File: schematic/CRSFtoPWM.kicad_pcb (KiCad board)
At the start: 4 copper layers, 44.4 x 21.5 mm, 29 parts, among them J1 Bat+, J2 UART1/Rx, J3 ICSP, J4 TSW-104-08-G-T-RA, J5 TSW-104-08-G-T-RA, J6 TSW-104-08-G-T-RA, J7 TSW-102-08-L-T-RA, U1 AP7375-50W5-7, U2 AP2210N-3.3TRG1, U3 ATSAMD21E18A-MU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

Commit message: Pcb fully routed - needs optimization
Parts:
- moved R3 0.20 mm to (163.7, 111.3)
- moved R2 0.10 mm to (146.2, 112.3)
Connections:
- J4 pad 1: SCL -> +3V3
- J4 pad 2: +3V3 -> +5V
- J4 pad 4: SDA -> TX2
- J4 pad 5: GND -> RX2
- J4 pad 6: +5V -> GND
- J4 pad 7: RX2 -> SCL
- J4 pad 8: TX2 -> SDA
- U3 pad 16: unconnected-(U3-Pad16) -> Net-(R6-Pad1)
- U3 pad 19: Net-(R6-Pad1) -> unconnected-(U3-Pad19)
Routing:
- net Vservo: track 0.00 -> 70.5 mm
- net Vbat: track 0.00 -> 26.5 mm
- net SDA: track 0.00 -> 25.3 mm, vias 0 -> 1
- net SCL: track 0.00 -> 24.0 mm, vias 0 -> 3
- net GND: track 0.00 -> 21.6 mm, vias 0 -> 14
- net Net-(J2-Pad3): track 0.00 -> 20.8 mm, vias 0 -> 2
- net Net-(R1-Pad2): track 0.00 -> 20.7 mm, vias 0 -> 2
- net Net-(J3-Pad1): track 0.00 -> 20.3 mm, vias 0 -> 1
- net RX2: track 0.00 -> 20.0 mm, vias 0 -> 1
- net CH9: track 0.00 -> 19.5 mm
- net Net-(J2-Pad4): track 0.00 -> 19.4 mm, vias 0 -> 2
- net +5V: track 0.00 -> 18.6 mm
- net CH10: track 0.00 -> 17.6 mm
- net CH8: track 0.00 -> 17.0 mm
- net TX2: track 0.00 -> 16.5 mm, vias 0 -> 1
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- added copper zone on In2.Cu, net +3V3
- added copper zone on In1.Cu, net GND
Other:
- board size 44.4 x 21.5 mm -> 43.9 x 21.5 mm

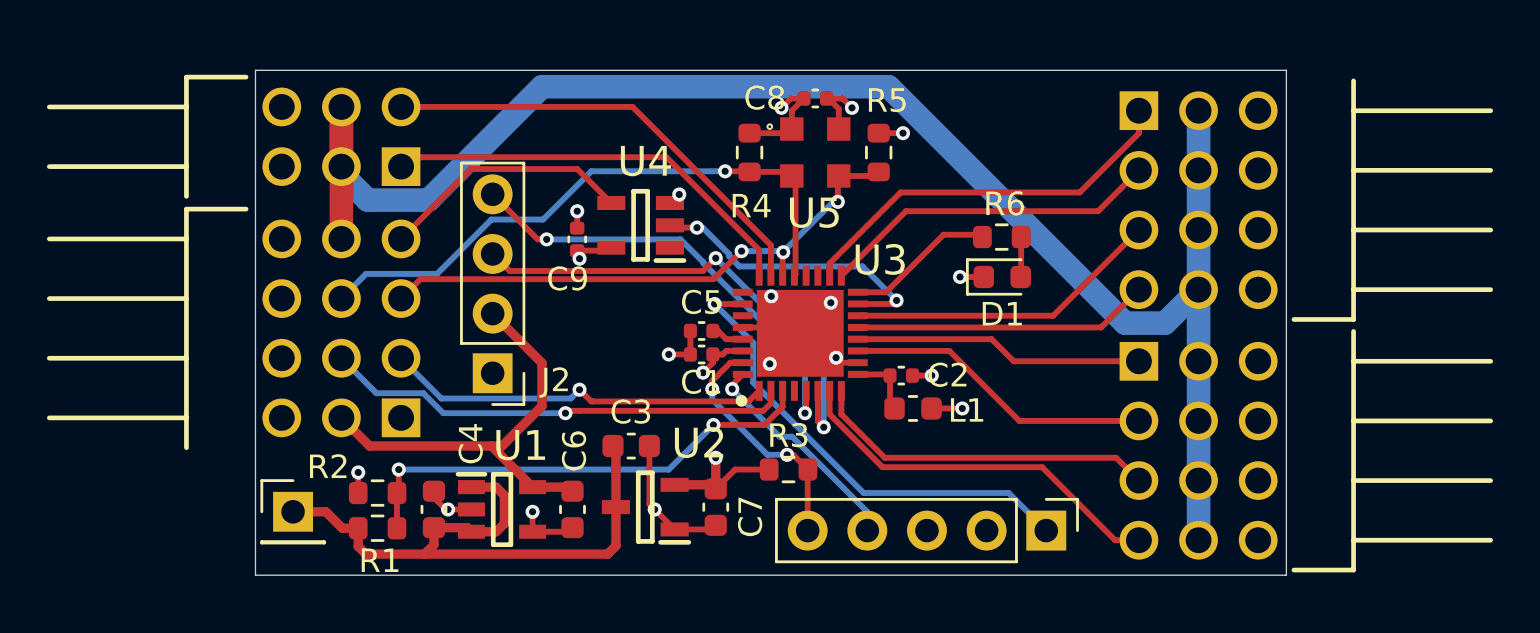
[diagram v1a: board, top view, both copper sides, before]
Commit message: Smaller pcb and tweaks
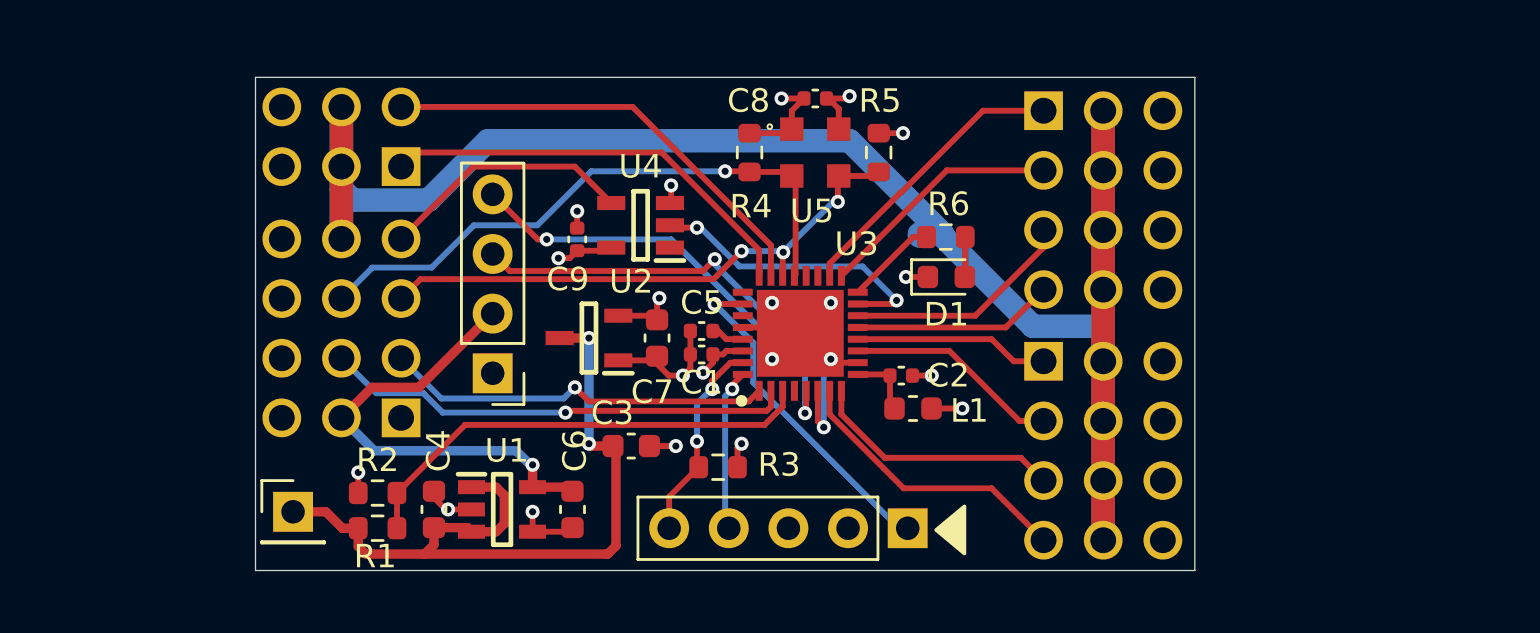
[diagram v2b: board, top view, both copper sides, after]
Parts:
- moved C7 7.62 mm to (158.1, 105.7)
- moved U2 7.59 mm to (155.2, 105.7)
- moved J3 5.90 mm to (168.8, 113.8)
- moved J5 4.06 mm to (174.6, 106.7)
- moved J6 4.06 mm to (174.6, 96.0)
- moved R3 3.00 mm to (160.7, 111.2), turned to 180 degrees
- moved D1 2.38 mm to (170.4, 103.1)
- moved R6 2.38 mm to (170.4, 101.4)
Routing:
- net Vservo: track 70.5 -> 84.8 mm
- net Vbat: track 26.5 -> 33.3 mm, vias 0 -> 2
- net Net-(U3-Pad26): track 20.3 -> 14.0 mm
- net CH8: track 17.0 -> 12.3 mm
- net CH5: track 16.4 -> 12.3 mm
- net CH7: track 14.5 -> 10.5 mm
- net CH6: track 14.8 -> 10.8 mm
- net CH3: track 12.6 -> 8.58 mm
- net CH2: track 12.4 -> 8.30 mm
- net CH1: track 13.2 -> 9.14 mm
- net CH4: track 13.5 -> 9.86 mm
- net Net-(J3-Pad4): track 9.53 -> 6.71 mm
- net Net-(R6-Pad1): track 6.22 -> 3.90 mm
- net Net-(J3-Pad5): track 10.3 -> 8.63 mm
- net +3V3: track 16.1 -> 14.5 mm, vias 6 -> 7
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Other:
- board size 43.9 x 21.5 mm -> 40 x 21 mm

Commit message: Added text, minor tweaks
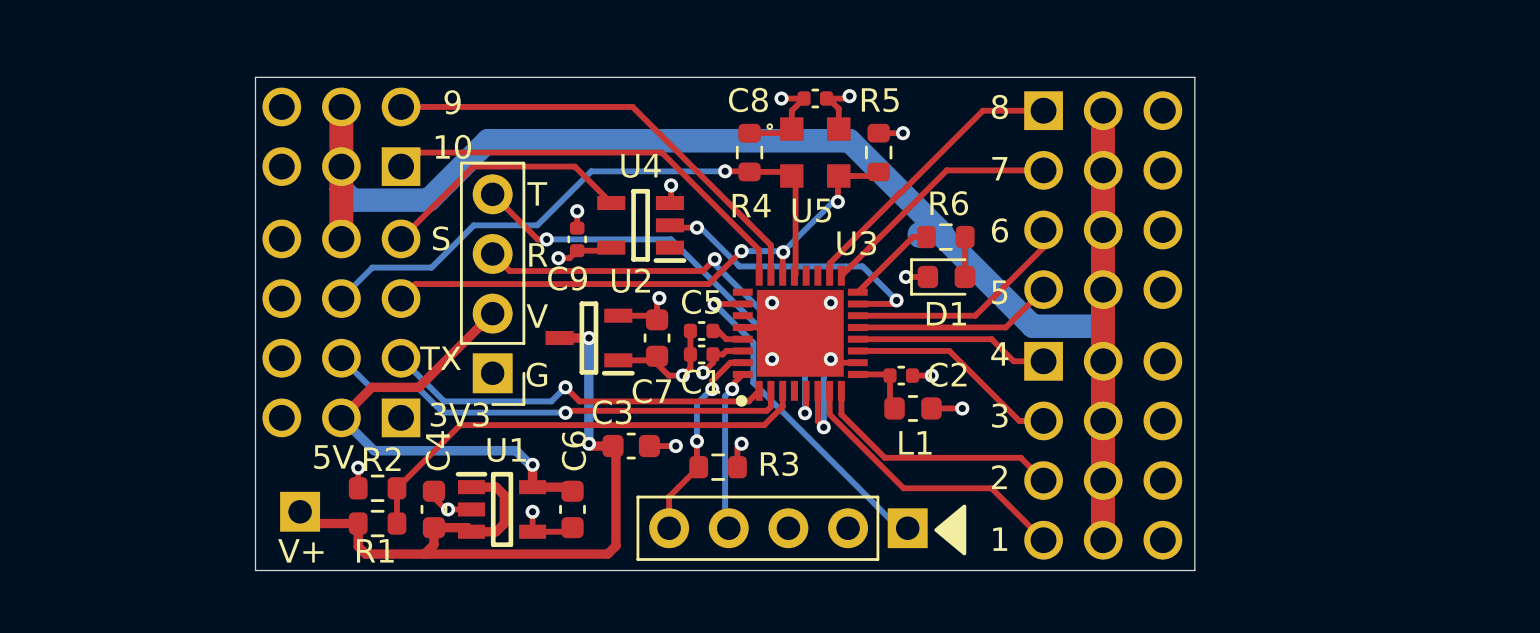
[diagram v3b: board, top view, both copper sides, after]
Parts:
- moved J1 0.30 mm to (142.9, 113.1)
- moved R1 0.20 mm to (146.2, 113.6)
- moved R2 0.20 mm to (146.2, 112.1)
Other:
- board text added: "+"
- board text added: "-"
- board text added: "1"
- board text added: "10"
- board text added: "2"
- board text added: "3"
- board text added: "3V3"
- board text added: "4"
- board text added: "5"
- board text added: "5V"
- board text added: "6"
- board text added: "7"
- board text added: "8"
- board text added: "9"
- board text added: "CRSFtoPWM"
- board text added: "G"
- board text added: "JLCJLCJLC"
- board text added: "R"
- board text added: "S"
- board text added: "T"
- board text added: "TX"
- board text added: "V"
- board text added: "V+"
- board text added: "V1.0 QES 2023"
- board text added: "s"

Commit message: Improved Vservo current capacity
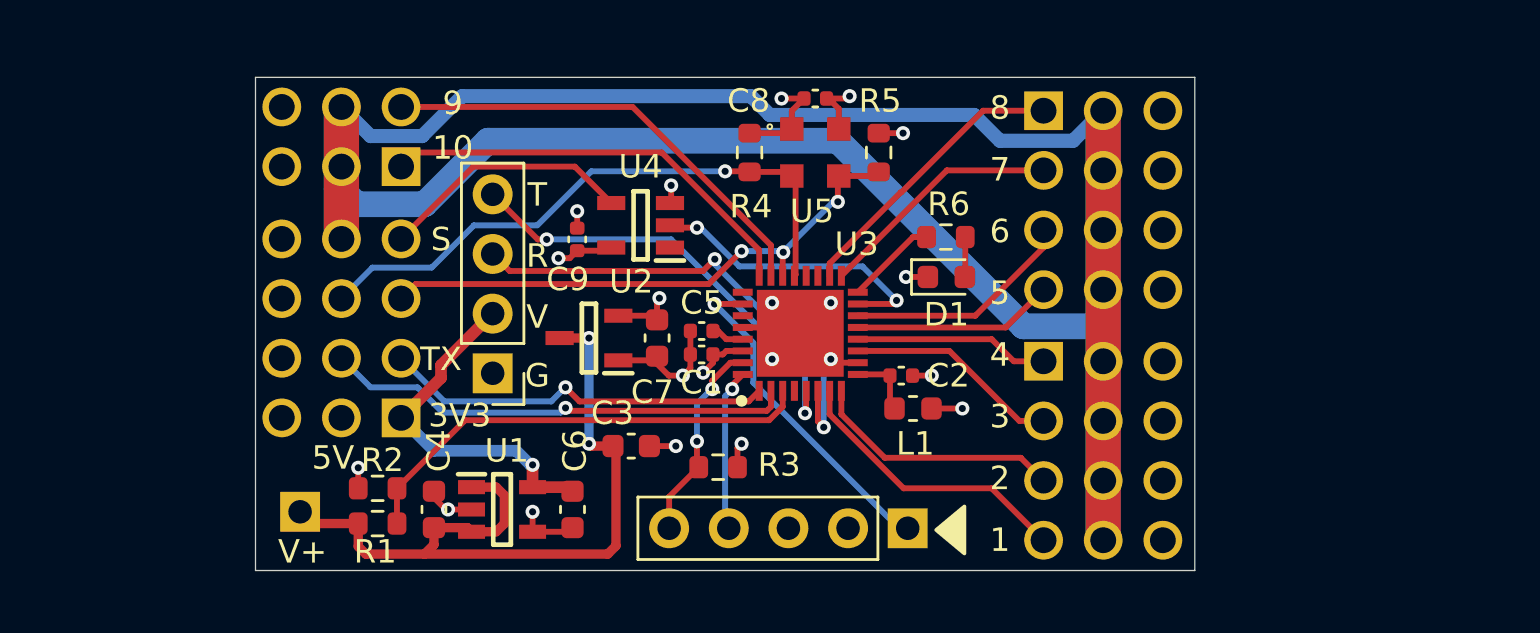
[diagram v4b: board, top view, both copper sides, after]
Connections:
- J4 pad 1: +3V3 -> +5V
- J4 pad 2: +5V -> +3V3
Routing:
- net Vservo: track 84.8 -> 119.9 mm
- net +5V: track 19.7 -> 15.0 mm
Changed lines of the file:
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@@
     (fp_line (start 8.89 -6.6) (end -1.27 -6.6) (layer "F.Fab") (width 0.1))
     (pad "1" thru_hole rect (at 0 0 90) (size 1.65 1.65) (drill 1.1) (layers *.Cu *.Mask)
-      (net 1 "+3V3") (pinfunction "1") (pintype "passive"))
+      (net 5 "+5V") (pinfunction "1") (pintype "passive"))
     (pad "2" thru_hole circle (at 0 -2.54 90) (size 1.65 1.65) (drill 1.1) (layers *.Cu *.Mask)
-      (net 5 "+5V") (pinfunction "2") (pintype "passive"))
+      (net 1 "+3V3") (pinfunction "2") (pintype "passive"))
     (pad "3" thru_hole circle (at 0 -5.08 90) (size 1.65 1.65) (drill 1.1) (layers *.Cu *.Mask)
       (net 30 "GND") (pinfunction "3") (pintype "passive"))
@@
   (segment (start 161.05 105.75) (end 161.75 105.75) (width 0.25) (layer "F.Cu") (net 4))
   (segment (start 160.7 105.4) (end 161.05 105.75) (width 0.25) (layer "F.Cu") (net 4))
-  (segment (start 152.8 112.05) (end 152.8 111.1) (width 0.4) (layer "F.Cu") (net 5))
-  (segment (start 152.8 112.05) (end 154.325 112.05) (width 0.4) (layer "F.Cu") (net 5))
-  (segment (start 144.66 109.1) (end 145.96 107.8) (width 0.4) (layer "F.Cu") (net 5))
-  (segment (start 145.96 107.8) (end 147.96 107.8) (width 0.4) (layer "F.Cu") (net 5))
-  (segment (start 147.96 107.8) (end 151.1 104.66) (width 0.4) (layer "F.Cu") (net 5))
+  (segment (start 152.8 112.05) (end 152.8 111.1) (width 0.5) (layer "F.Cu") (net 5))
+  (segment (start 148.9 106.86) (end 151.1 104.66) (width 0.5) (layer "F.Cu") (net 5))
+  (segment (start 152.8 112.05) (end 154.325 112.05) (width 0.5) (layer "F.Cu") (net 5))
+  (segment (start 148.9 107.4) (end 148.9 106.86) (width 0.5) (layer "F.Cu") (net 5))
+  (segment (start 147.2 109.1) (end 148.9 107.4) (width 0.5) (layer "F.Cu") (net 5))
   (via (at 152.8 111.1) (size 0.6) (drill 0.3) (layers "F.Cu" "B.Cu") (net 5))
-  (segment (start 152.1 110.5) (end 146.06 110.5) (width 0.4) (layer "B.Cu") (net 5))
-  (segment (start 152.8 111.1) (end 152.7 111.1) (width 0.4) (layer "B.Cu") (net 5))
-  (segment (start 146.06 110.5) (end 144.66 109.1) (width 0.4) (layer "B.Cu") (net 5))
-  (segment (start 152.7 111.1) (end 152.1 110.5) (width 0.4) (layer "B.Cu") (net 5))
+  (segment (start 148.6 110.5) (end 147.2 109.1) (width 0.5) (layer "B.Cu") (net 5))
+  (segment (start 152.8 111.1) (end 152.7 111.1) (width 0.5) (layer "B.Cu") (net 5))
+  (segment (start 152.1 110.5) (end 148.6 110.5) (width 0.5) (layer "B.Cu") (net 5))
+  (segment (start 152.7 111.1) (end 152.1 110.5) (width 0.5) (layer "B.Cu") (net 5))
   (segment (start 171.225 101.4) (end 171.225 103.0825) (width 0.25) (layer "F.Cu") (net 6))
   (segment (start 160.054501 102.845499) (end 160.558244 102.341756) (width 0.25) (layer "F.Cu") (net 7))
@@
   (segment (start 171.652557 104.75) (end 174.56 101.842557) (width 0.25) (layer "F.Cu") (net 15))
   (segment (start 166.65 104.75) (end 171.652557 104.75) (width 0.25) (layer "F.Cu") (net 15))
-  (segment (start 147.025 112.1) (end 149.716564 109.408436) (width 0.25) (layer "F.Cu") (net 16))
+  (segment (start 162.875 109.2) (end 163.45 108.625) (width 0.25) (layer "F.Cu") (net 16))
   (segment (start 147.025 113.6) (end 147.025 112.1) (width 0.25) (layer "F.Cu") (net 16))
-  (segment (start 149.716564 109.408436) (end 162.666564 109.408436) (width 0.25) (layer "F.Cu") (net 16))
-  (segment (start 162.666564 109.408436) (end 163.45 108.625) (width 0.25) (layer "F.Cu") (net 16))
+  (segment (start 147.025 112.1) (end 149.925 109.2) (width 0.25) (layer "F.Cu") (net 16))
+  (segment (start 149.925 109.2) (end 162.875 109.2) (width 0.25) (layer "F.Cu") (net 16))
   (segment (start 163.45 108.625) (end 163.45 107.95) (width 0.25) (layer "F.Cu") (net 16))
   (segment (start 170.44 98.56) (end 174.56 98.56) (width 0.25) (layer "F.Cu") (net 17))
@@
   (segment (start 166.850499 102.650499) (end 161.608743 102.650499) (width 0.25) (layer "B.Cu") (net 23))
   (segment (start 168.3 104.1) (end 166.850499 102.650499) (width 0.25) (layer "B.Cu") (net 23))
-  (segment (start 144.66 95.86) (end 144.66 101.48) (width 1) (layer "F.Cu") (net 29))
-  (segment (start 177.1 96.02) (end 177.1 114.31) (width 1) (layer "F.Cu") (net 29))
-  (segment (start 145.125 99.825) (end 144.66 99.36) (width 1) (layer "B.Cu") (net 29))
-  (segment (start 177.1 105.2) (end 177.1 114.31) (width 1) (layer "B.Cu") (net 29))
-  (segment (start 170.264494 101.359749) (end 174.104745 105.2) (width 1) (layer "B.Cu") (net 29))
-  (segment (start 144.66 99.36) (end 144.66 101.48) (width 1) (layer "B.Cu") (net 29))
-  (segment (start 177.1 96.02) (end 177.1 105.2) (width 1) (layer "B.Cu") (net 29))
-  (segment (start 169.271994 101.359749) (end 169.271994 101.263994) (width 1) (layer "B.Cu") (net 29))
-  (segment (start 150.89975 97.29975) (end 148.3745 99.825) (width 1) (layer "B.Cu") (net 29))
-  (segment (start 144.66 95.86) (end 144.66 99.36) (width 1) (layer "B.Cu") (net 29))
-  (segment (start 166.30025 97.29975) (end 150.89975 97.29975) (width 1) (layer "B.Cu") (net 29))
-  (segment (start 174.104745 105.2) (end 177.1 105.2) (width 1) (layer "B.Cu") (net 29))
-  (segment (start 148.3745 99.825) (end 145.125 99.825) (width 1) (layer "B.Cu") (net 29))
-  (segment (start 170.264494 101.263994) (end 166.30025 97.29975) (width 1) (layer "B.Cu") (net 29))
+  (segment (start 144.66 95.86) (end 144.66 101.48) (width 1.5) (layer "F.Cu") (net 29))
+  (segment (start 177.1 96.02) (end 177.1 114.31) (width 1.5) (layer "F.Cu") (net 29))
+  (segment (start 162.1 95.4) (end 149.8 95.4) (width 0.6) (layer "B.Cu") (net 29))
+  (segment (start 177.1 105.2) (end 177.1 114.31) (width 1.5) (layer "B.Cu") (net 29))
+  (segment (start 150.89975 97.29975) (end 165.79975 97.29975) (width 1.1) (layer "B.Cu") (net 29))
+  (segment (start 177.1 96.02) (end 175.82 97.3) (width 0.6) (layer "B.Cu") (net 29))
+  (segment (start 144.66 99.36) (end 144.66 101.48) (width 1.5) (layer "B.Cu") (net 29))
+  (segment (start 177.1 96.02) (end 177.1 105.2) (width 1.5) (layer "B.Cu") (net 29))
+  (segment (start 162.9 96.2) (end 162.1 95.4) (width 0.6) (layer "B.Cu") (net 29))
+  (segment (start 148.1 97.1) (end 145.9 97.1) (width 0.6) (layer "B.Cu") (net 29))
+  (segment (start 148.1995 100) (end 150.89975 97.29975) (width 1.1) (layer "B.Cu") (net 29))
+  (segment (start 144.66 95.86) (end 144.66 99.36) (width 1.5) (layer "B.Cu") (net 29))
+  (segment (start 145.9 97.1) (end 144.66 95.86) (width 0.6) (layer "B.Cu") (net 29))
+  (segment (start 149.8 95.4) (end 148.1 97.1) (width 0.6) (layer "B.Cu") (net 29))
+  (segment (start 171.6 96.2) (end 162.9 96.2) (width 0.6) (layer "B.Cu") (net 29))
+  (segment (start 144.66 99.36) (end 145.3 100) (width 1.1) (layer "B.Cu") (net 29))
+  (segment (start 172.7 97.3) (end 171.6 96.2) (width 0.6) (layer "B.Cu") (net 29))
+  (segment (start 173.7 105.2) (end 177.1 105.2) (width 1.1) (layer "B.Cu") (net 29))
+  (segment (start 145.3 100) (end 148.1995 100) (width 1.1) (layer "B.Cu") (net 29))
+  (segment (start 175.82 97.3) (end 172.7 97.3) (width 0.6) (layer "B.Cu") (net 29))
+  (segment (start 165.79975 97.29975) (end 173.7 105.2) (width 1.1) (layer "B.Cu") (net 29))
   (segment (start 149.2 113) (end 150.2 113) (width 0.25) (layer "F.Cu") (net 30))
   (segment (start 158.1 106.8) (end 158.6 107.3) (width 0.25) (layer "F.Cu") (net 30))
@@
   (segment (start 149.04 108.4) (end 153.6 108.4) (width 0.25) (layer "B.Cu") (net 32))
   (segment (start 147.2 106.56) (end 149.04 108.4) (width 0.25) (layer "B.Cu") (net 32))
+  (segment (start 162.775 108.8) (end 154.328026 108.8) (width 0.25) (layer "F.Cu") (net 33))
+  (segment (start 154.328026 108.8) (end 154.203526 108.6755) (width 0.25) (layer "F.Cu") (net 33))
+  (segment (start 162.95 107.95) (end 162.95 108.625) (width 0.25) (layer "F.Cu") (net 33))
   (segment (start 162.95 108.625) (end 162.775 108.8) (width 0.25) (layer "F.Cu") (net 33))
-  (segment (start 162.775 108.8) (end 154.287462 108.8) (width 0.25) (layer "F.Cu") (net 33))
-  (segment (start 162.95 107.95) (end 162.95 108.625) (width 0.25) (layer "F.Cu") (net 33))
-  (segment (start 154.287462 108.8) (end 154.203526 108.883936) (width 0.25) (layer "F.Cu") (net 33))
-  (via (at 154.203526 108.883936) (size 0.6) (drill 0.3) (layers "F.Cu" "B.Cu") (net 33))
-  (segment (start 148.9755 108.8755) (end 154.19509 108.8755) (width 0.25) (layer "B.Cu") (net 33))
+  (via (at 154.203526 108.6755) (size 0.6) (drill 0.3) (layers "F.Cu" "B.Cu") (net 33))
+  (segment (start 148.9755 108.8755) (end 154.003526 108.8755) (width 0.25) (layer "B.Cu") (net 33))
+  (segment (start 154.003526 108.8755) (end 154.203526 108.6755) (width 0.25) (layer "B.Cu") (net 33))
   (segment (start 147.9 107.8) (end 148.9755 108.8755) (width 0.25) (layer "B.Cu") (net 33))
   (segment (start 144.66 106.56) (end 145.9 107.8) (width 0.25) (layer "B.Cu") (net 33))
-  (segment (start 154.19509 108.8755) (end 154.203526 108.883936) (width 0.25) (layer "B.Cu") (net 33))
   (segment (start 145.9 107.8) (end 147.9 107.8) (width 0.25) (layer "B.Cu") (net 33))
   (segment (start 161 98.6) (end 162.014 98.6) (width 0.25) (layer "F.Cu") (net 34))

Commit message: Improved Rx,Tx traces
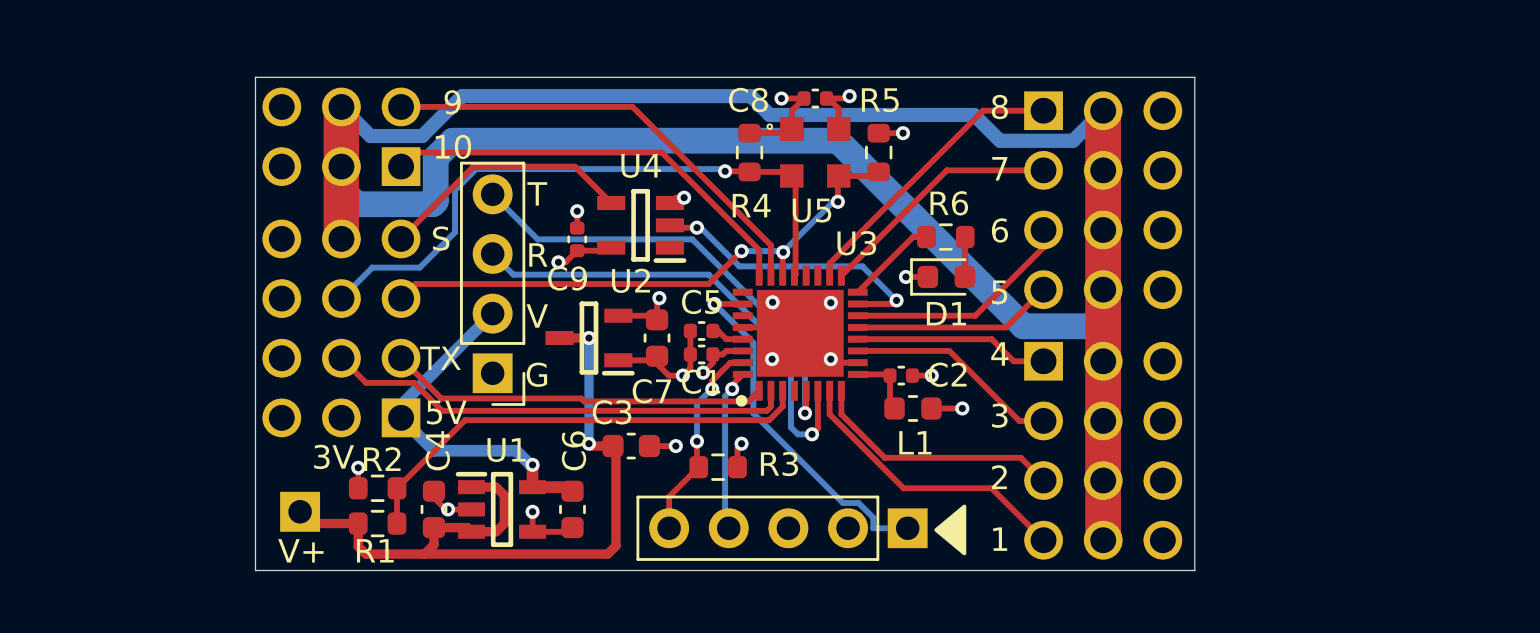
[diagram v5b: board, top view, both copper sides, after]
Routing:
- net SDA: track 25.3 -> 26.4 mm
- net Vservo: track 119.9 -> 121.0 mm
- net Net-(J3-Pad1): track 14.0 -> 15.0 mm
- net Vbat: track 33.1 -> 32.4 mm
- net +5V: track 15.0 -> 14.4 mm
- net Net-(J2-Pad4): track 19.1 -> 19.7 mm, vias 2 -> 1
- net TX2: track 16.7 -> 16.2 mm, vias 1 -> 0
- net Net-(J2-Pad3): track 20.7 -> 20.5 mm, vias 2 -> 1
- net RX2: track 20.1 -> 20.0 mm, vias 1 -> 0
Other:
- board text added: "3V"
- board text removed: "3V3"
